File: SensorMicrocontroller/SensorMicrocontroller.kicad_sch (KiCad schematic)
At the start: 45 parts, among them J1 JST B4B-PH-SM4-TB, J2 JST B4B-PH-SM4-TB, J3 JST B6B-PH-SM4-TB, J4 JST B4B-PH-SM4-TB, J5 JST B4B-PH-SM4-TB, J8 12V Connector, J9 Light Connector, Q1 DMT6009LCT, Q2 DMT6009LCT, U1 ADS1115IDGS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

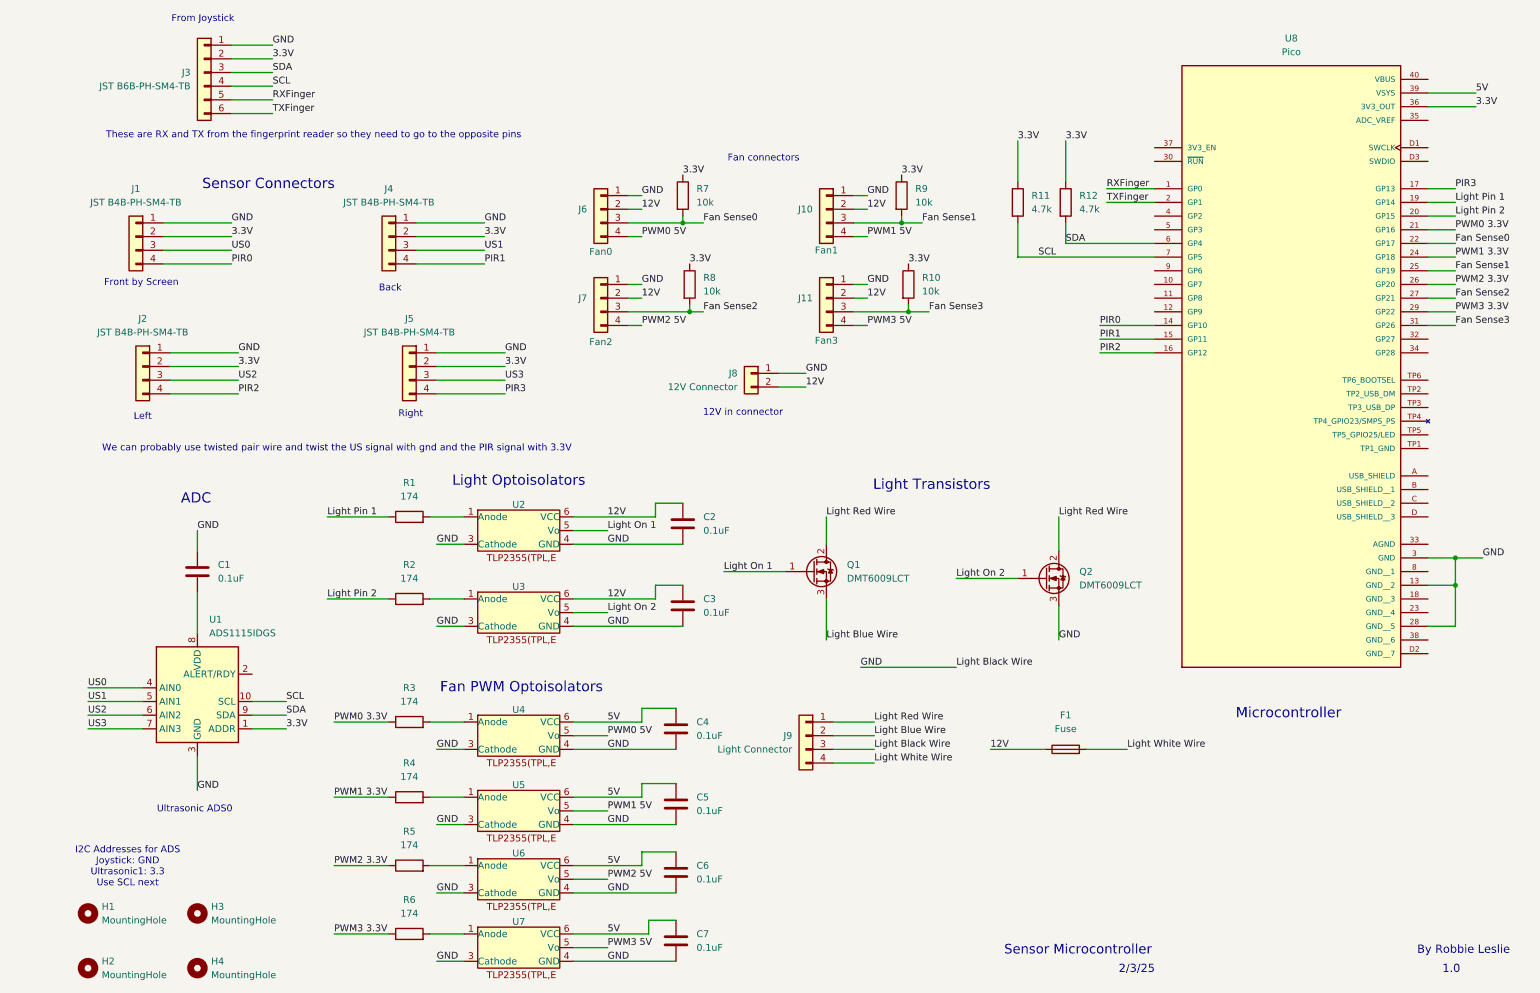
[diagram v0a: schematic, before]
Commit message: Removed fan optoisolators after testing them
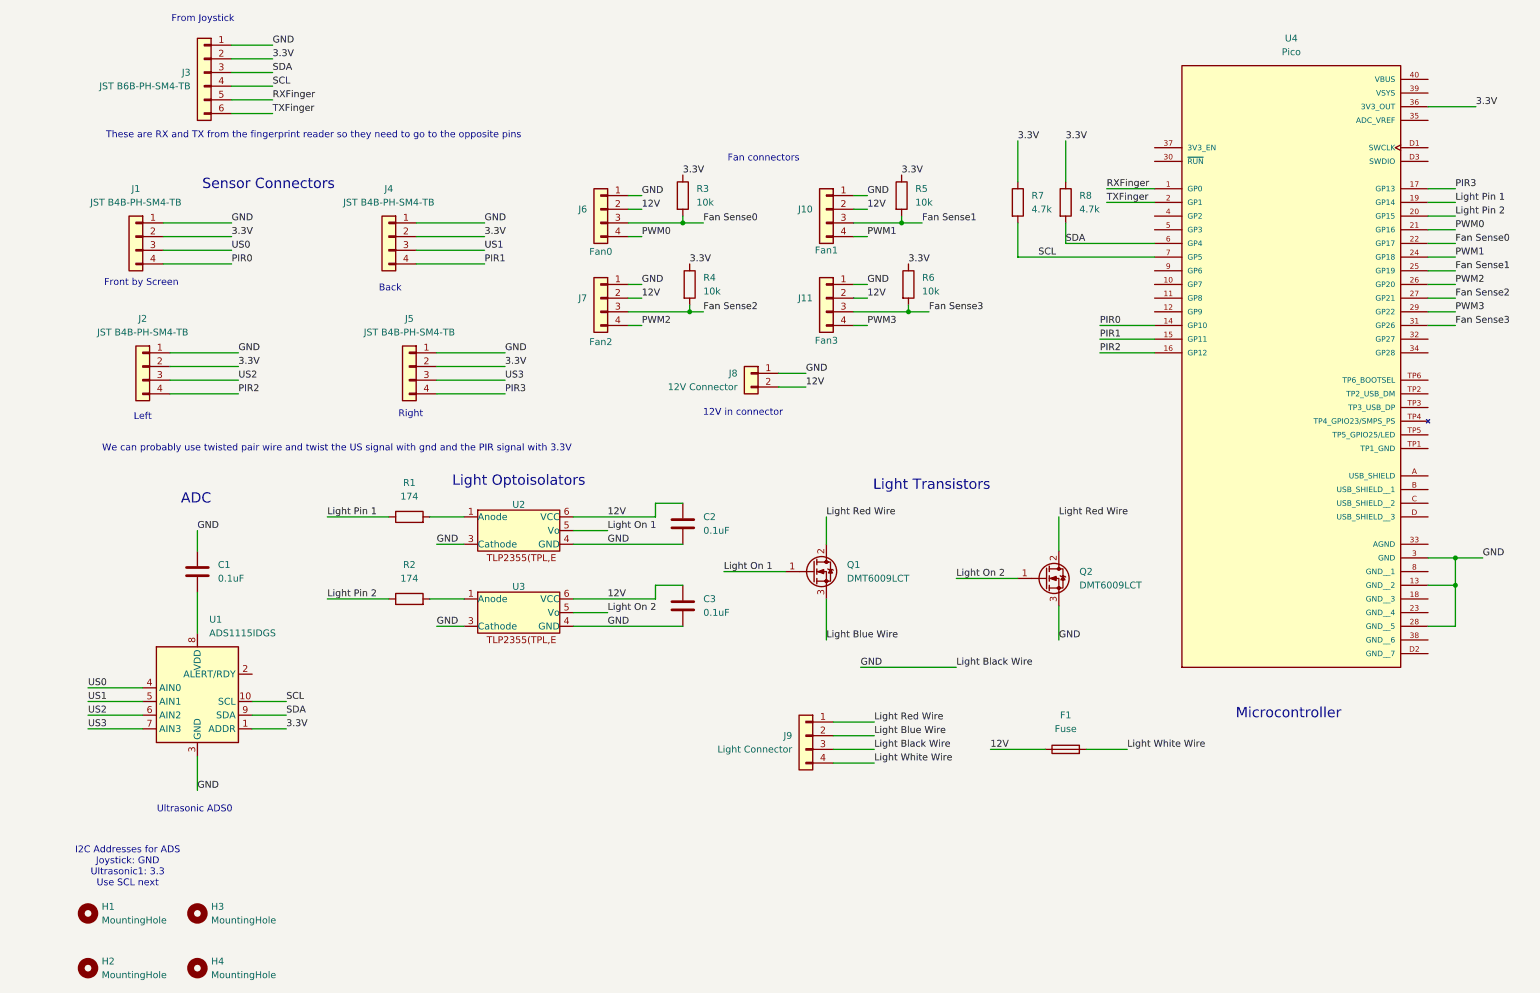
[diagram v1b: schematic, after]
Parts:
- removed C4, C5, C6, C7: 0.1uF, Capacitor_SMD:C_0805_2012Metric, symbol Device:C
- removed R3, R4, R5, R6: 174, Resistor_SMD:R_0805_2012Metric, symbol Device:R
- removed U4, U5, U6, U7: Optoisolators, Package_SO:SO-5-6_4.55x3.7mm_P1.27mm, symbol OptoIsolators:TLP2355(TPL,E
- U4: renamed from U8; footprint Footprints:pico -> CustomFootprints:pico
- renumbered R7 to R3, R8 to R4, R9 to R5, R10 to R6, R11 to R7, R12 to R8
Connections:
- net PWM0 5V is gone; now on net PWM0: J6.4 (Pin_4)
- net PWM1 5V is gone; now on net PWM1: J10.4 (Pin_4)
- net PWM2 5V is gone; now on net PWM2: J7.4 (Pin_4)
- net PWM3 5V is gone; now on net PWM3: J11.4 (Pin_4)
- net 5V: no longer names the net of U4.39 (VSYS)
- net PWM0 3.3V renamed PWM0
- net PWM1 3.3V renamed PWM1
- net PWM2 3.3V renamed PWM2
- net PWM3 3.3V renamed PWM3
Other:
- note removed: "1.0"
- note removed: "2/3/25"
- note removed: "By Robbie Leslie"
- note removed: "Fan PWM Optoisolators"
- note removed: "Sensor Microcontroller"
- company: (none) -> Lafayette College
- title: (none) -> Sensor Microcontroller PCB
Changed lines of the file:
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@@
 	(generator_version "8.0")
 	(paper "A4")
+	(title_block
+		(title "Sensor Microcontroller PCB")
+		(date "2025-02-05")
+		(rev "v1.0")
+		(company "Lafayette College")
+		(comment 1 "By Robbie Leslie")
+	)

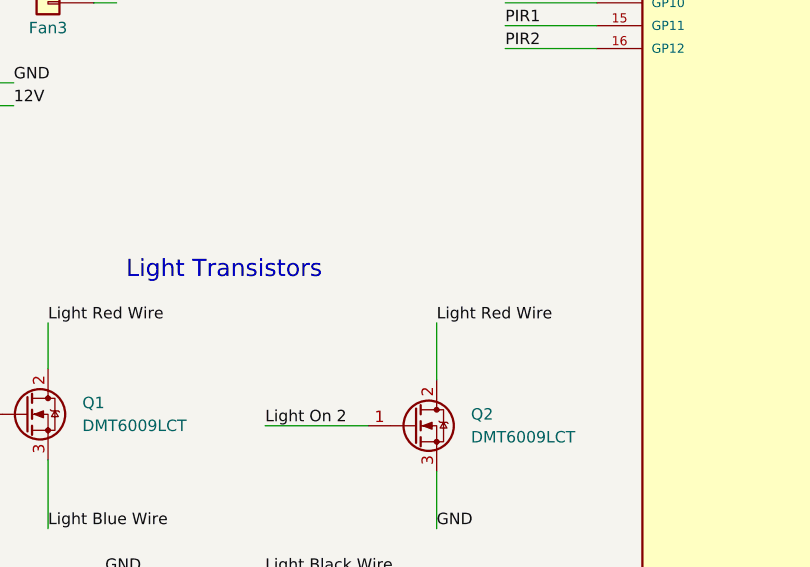
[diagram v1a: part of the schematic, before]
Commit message: Added pull up for light transistor after testing
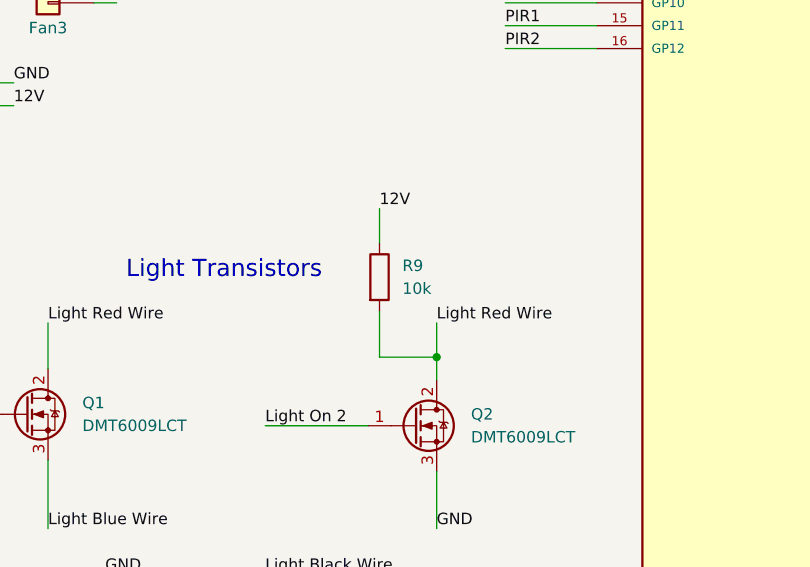
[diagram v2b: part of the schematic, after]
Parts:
- added R9: 10k, Resistor_SMD:R_0805_2012Metric, symbol Device:R
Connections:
- net 12V: now also R9.1
- net Light Red Wire: now also R9.2
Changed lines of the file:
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@@
 	(title_block
 		(title "Sensor Microcontroller PCB")
-		(date "2025-02-05")
+		(date "2025-02-07")
 		(rev "v1.0")
 		(company "Lafayette College")

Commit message: Fixed ADS1115 footprint
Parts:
- U1: footprint Package_SO:TSSOP-10_3x3mm_P0.5mm -> Package_SO:VSSOP-10_3x3mm_P0.5mm
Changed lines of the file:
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@@
 	(title_block
 		(title "Sensor Microcontroller PCB")
-		(date "2025-02-07")
+		(date "2025-02-08")
 		(rev "v1.0")
 		(company "Lafayette College")

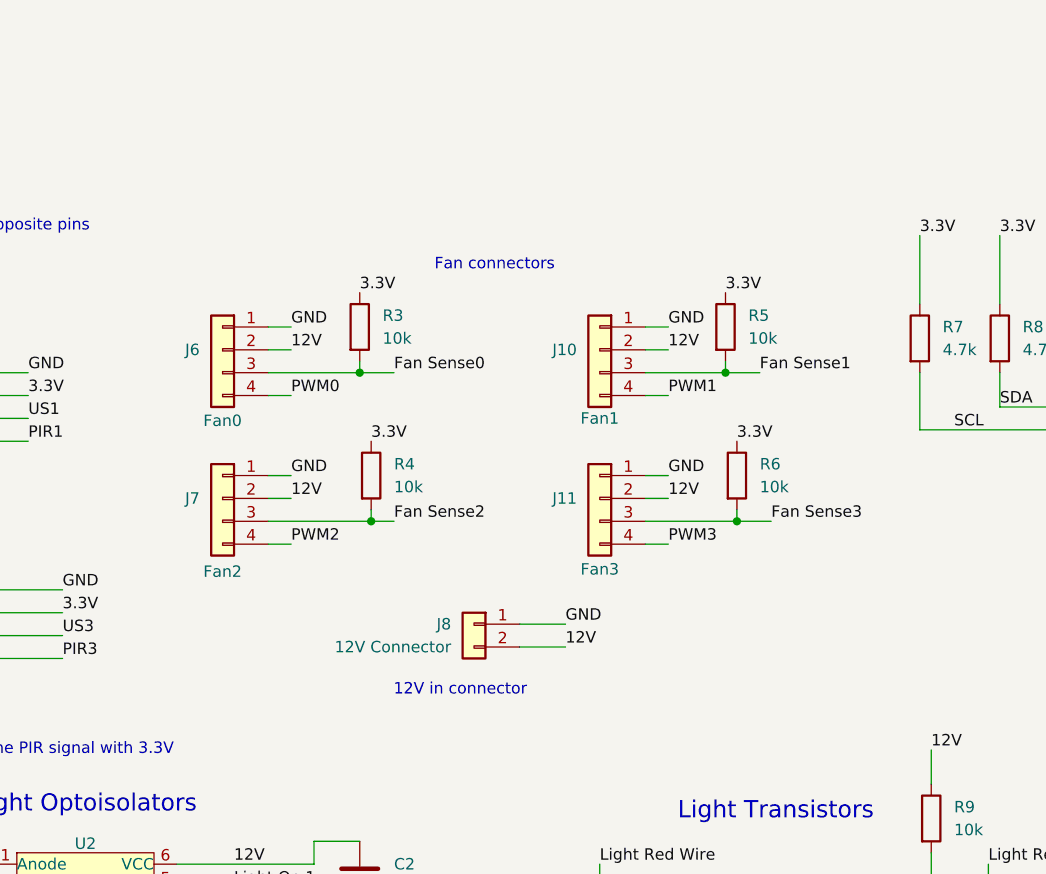
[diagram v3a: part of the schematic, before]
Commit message: Added cap for fan tach
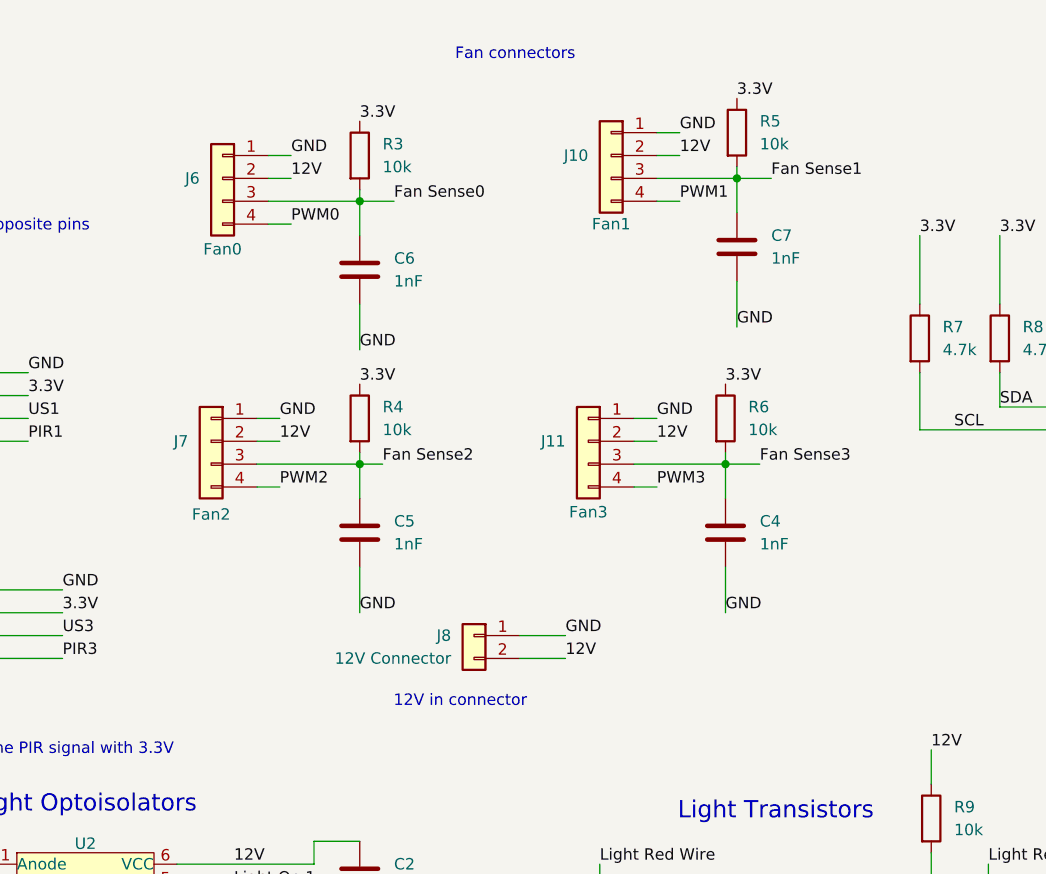
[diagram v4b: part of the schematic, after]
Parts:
- added C4, C5, C6, C7: 1nF, Capacitor_SMD:C_0805_2012Metric, symbol Device:C
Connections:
- net Fan Sense0: now also C6.1
- net Fan Sense1: now also C7.1
- net Fan Sense2: now also C5.1
- net Fan Sense3: now also C4.1
- net GND: now also C4.2, C5.2, C6.2, C7.2
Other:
- moved on the sheet: J10, J11, J6, J7, J8, R3, R4, R5, R6
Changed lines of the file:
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@@
 	(title_block
 		(title "Sensor Microcontroller PCB")
-		(date "2025-02-08")
+		(date "2025-02-11")
 		(rev "v1.0")
 		(company "Lafayette College")

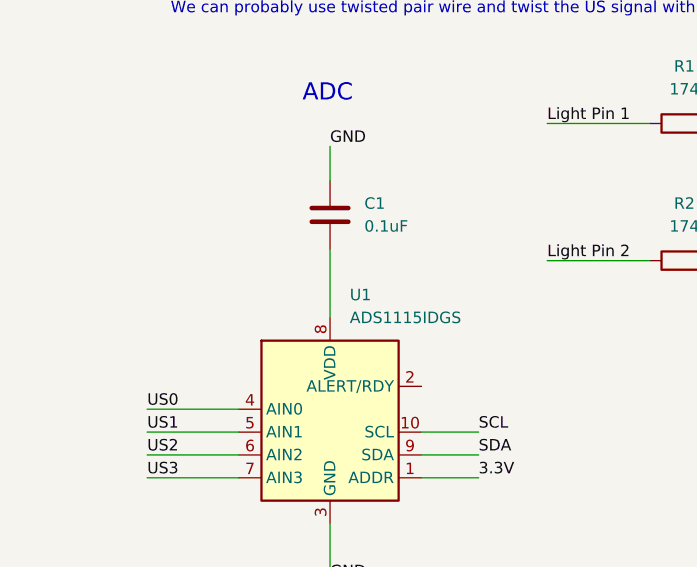
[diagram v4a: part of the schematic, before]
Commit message: Fixed power error on ADC
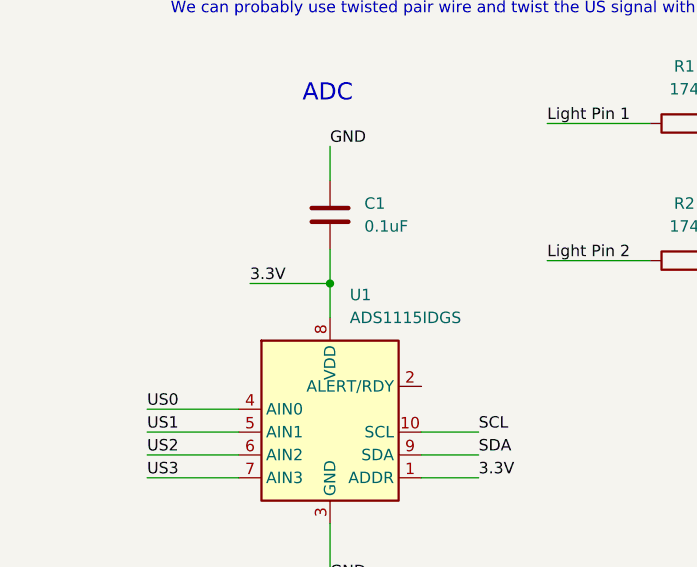
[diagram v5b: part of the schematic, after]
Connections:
- net 3.3V: now also C1.2, U1.8 (VDD)

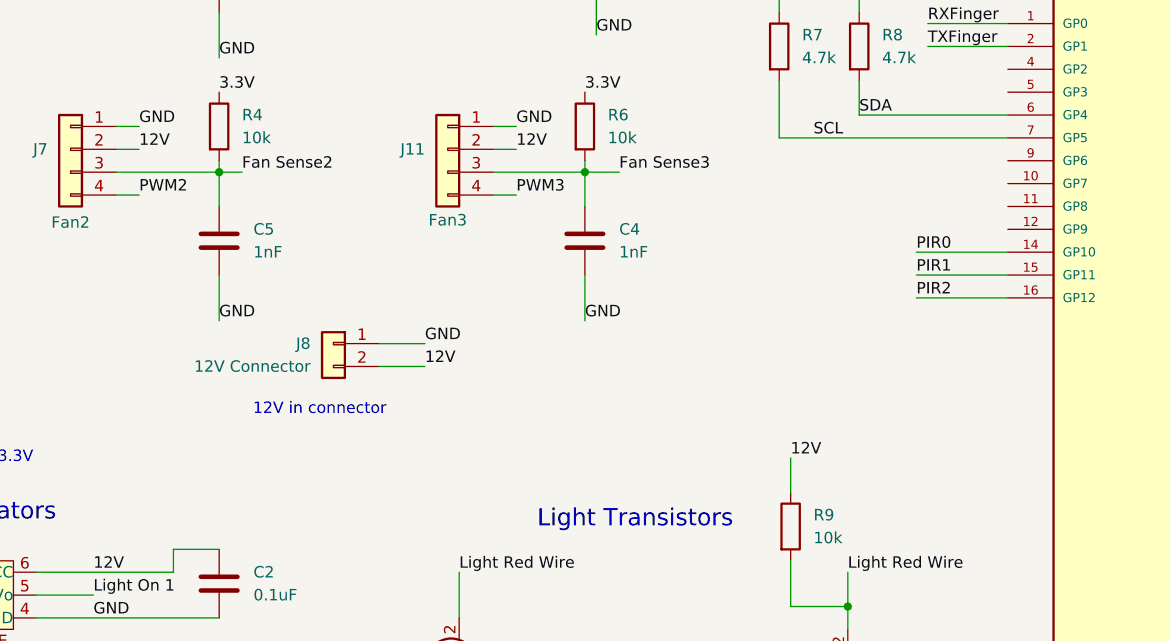
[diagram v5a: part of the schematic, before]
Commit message: Added LiDAR power controller
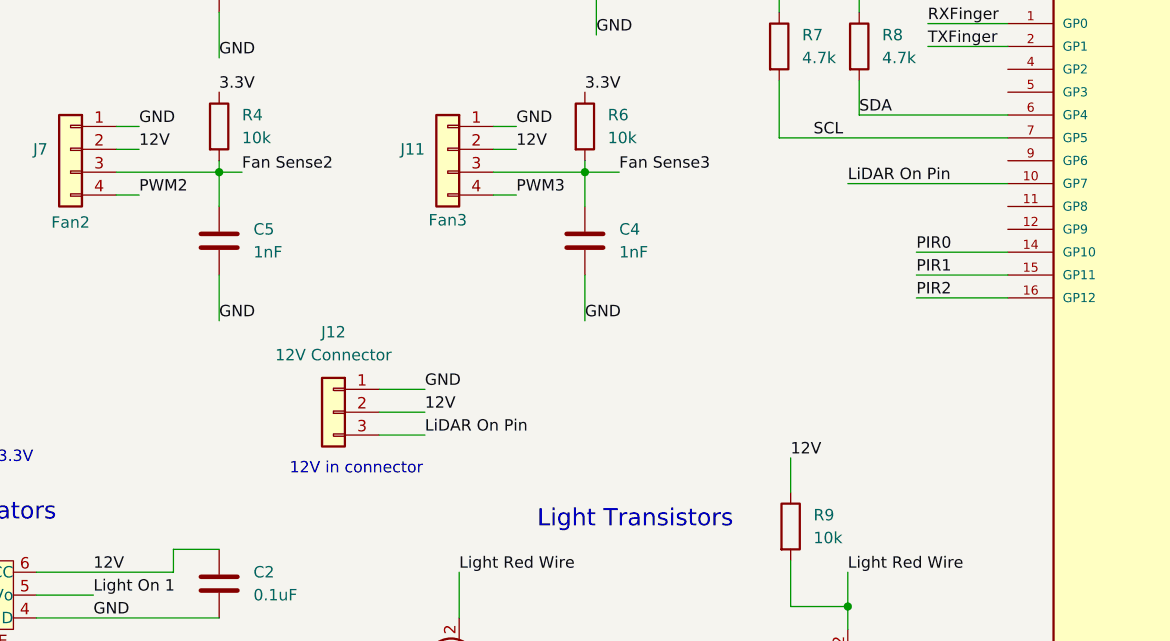
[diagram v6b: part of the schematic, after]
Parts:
- removed J8: 12V Connector, Connector_JST:JST_PH_B2B-PH-SM4-TB_1x02-1MP_P2.00mm_Vertical, symbol Connector_Generic:Conn_01x02
- added J12: 12V Connector, Connector_JST:JST_PH_B3B-PH-SM4-TB_1x03-1MP_P2.00mm_Vertical, symbol Connector_Generic:Conn_01x03
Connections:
- net 12V: now also J12.2 (Pin_2)
- net GND: now also J12.1 (Pin_1)
- net LiDAR On Pin: now reaches U4.10 (GP7)
- net LiDAR On Pin: now also J12.3 (Pin_3)

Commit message: Updated SensorMicrocontroller design
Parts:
- removed F1: Fuse, Fuse:Fuse_0805_2012Metric, symbol Device:Fuse
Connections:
- net Light White Wire is gone; now on net 12V: J9.4 (Pin_4)
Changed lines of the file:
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@@
 	(title_block
 		(title "Sensor Microcontroller PCB")
-		(date "2025-03-07")
+		(date "2025-03-12")
 		(rev "v1.1")
 		(company "Lafayette College")
